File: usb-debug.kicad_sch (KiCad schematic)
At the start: 86 parts, among them IC1 AP22652W6-7, IC15 TPS7A0518PDBVT, IC16 AP22653W6-7, IC7 HD3SS3220, J11 632723300011, T10 BSS138APW, T6 BSS138APW, T7 BSS138APW, T9 BSS138APW

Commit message: Update local libraries
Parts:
- IC1: footprint antmicro-footprints:SOT-23-6 -> jetson-nano-baseboard-footprints:SOT-23-6; symbol antmicroPMICPowerDistributionSwitchesLoadDrivers:AP22652W6-7 -> jetson-nano-baseboard:AP22652W6-7

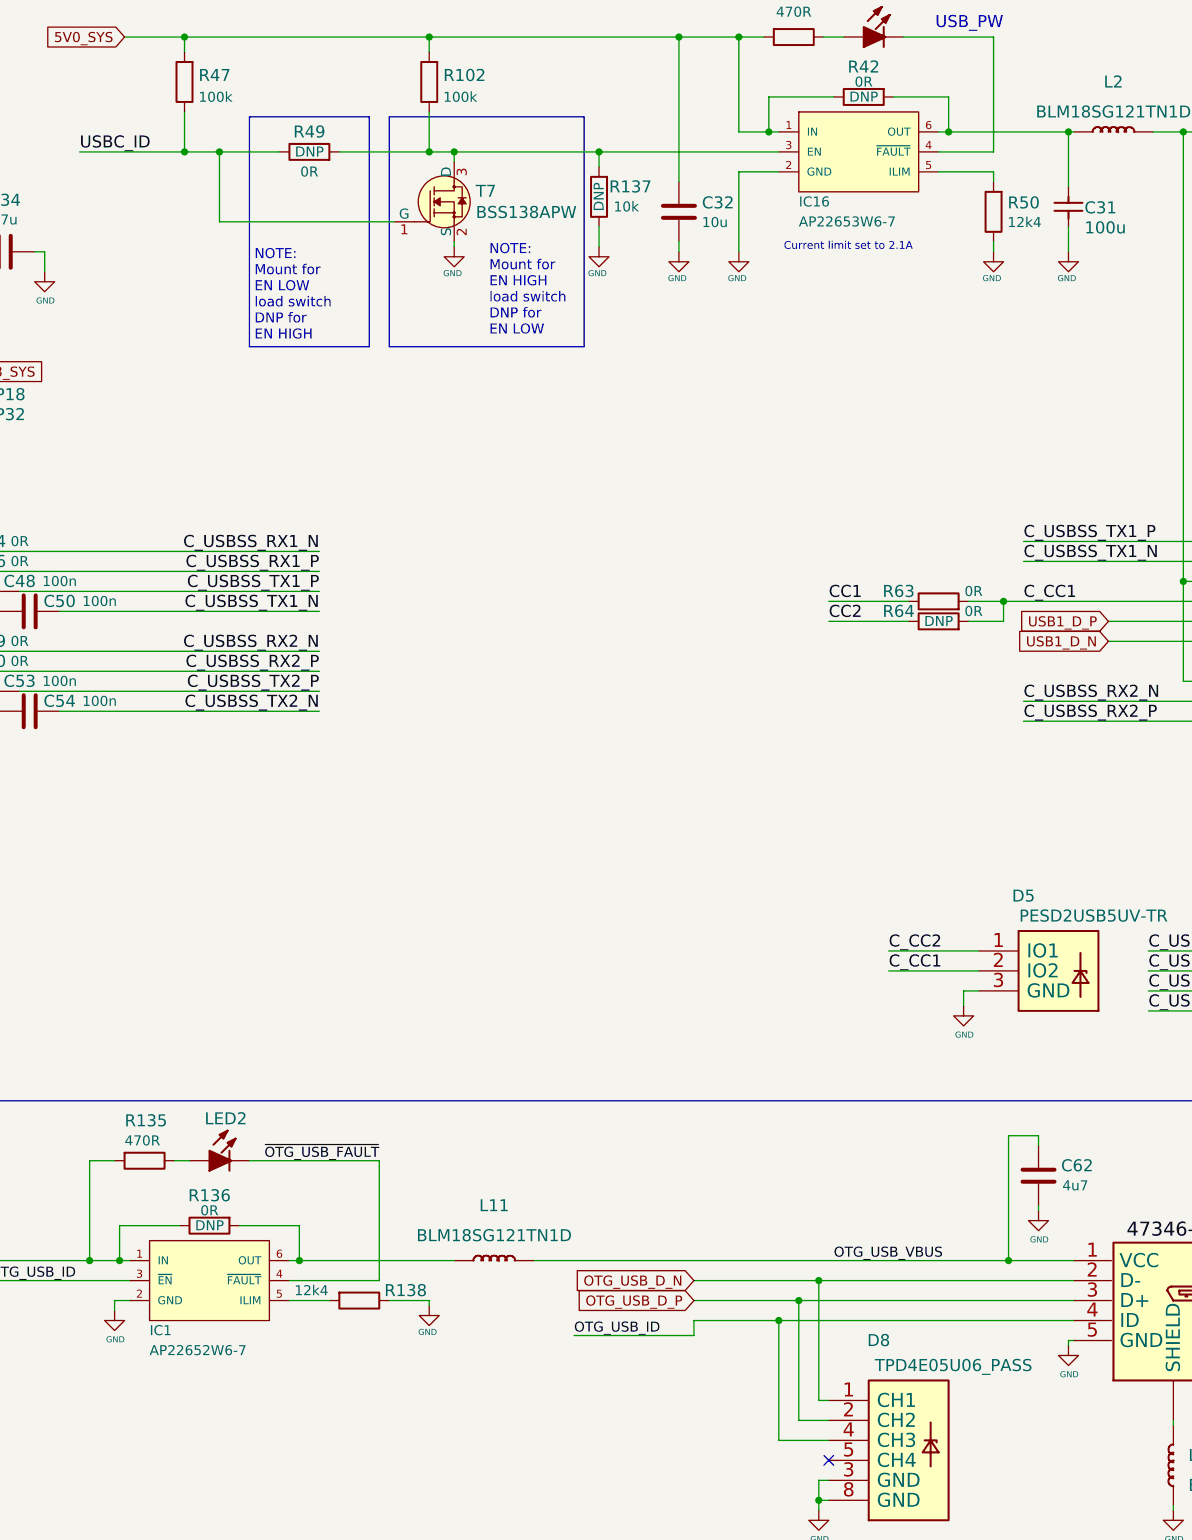
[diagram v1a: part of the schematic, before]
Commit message: Replace USB power switches with version without output discharge
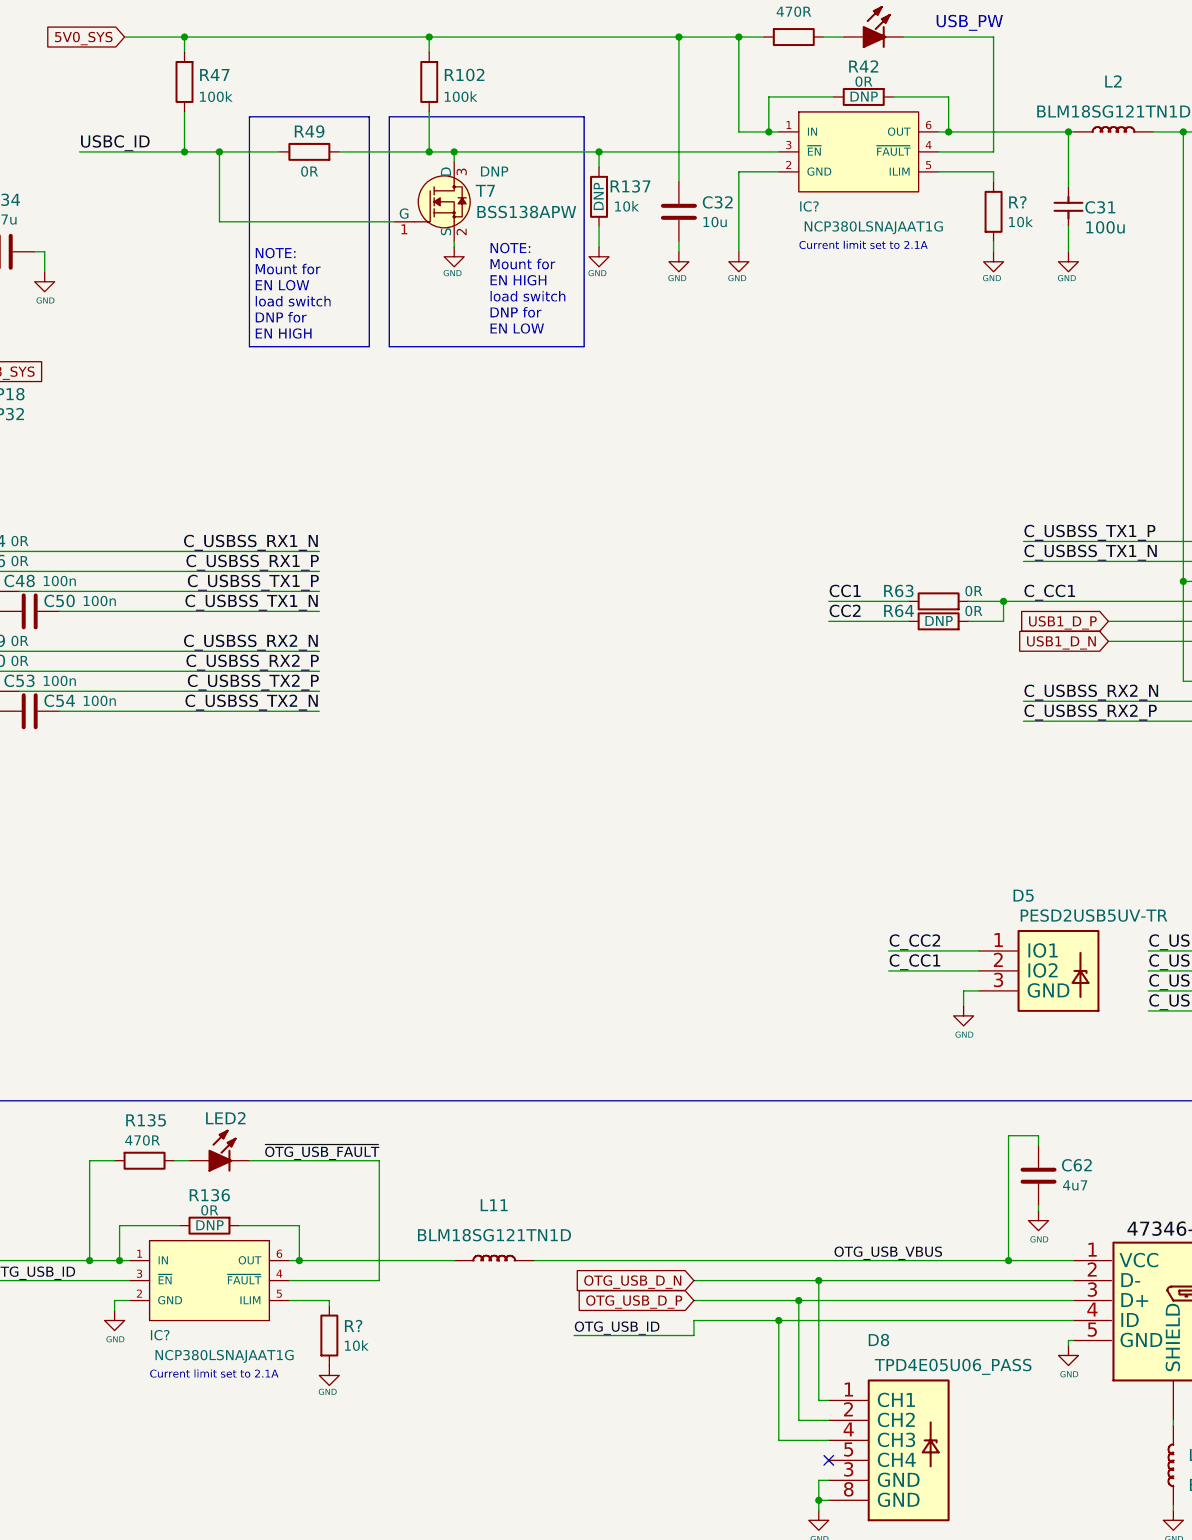
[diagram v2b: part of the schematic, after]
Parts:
- removed IC1: AP22652W6-7, jetson-nano-baseboard-footprints:SOT-23-6, symbol jetson-nano-baseboard:AP22652W6-7
- removed IC16: AP22653W6-7, jetson-nano-baseboard-footprints:SOT-23-6, symbol jetson-nano-baseboard:AP22653W6-7
- removed R138, R50: R_12k4_0402, jetson-nano-baseboard-footprints:0402-res, symbol jetson-nano-baseboard:R_12k4_0402
- added IC? (x2): NCP380LSNAJAAT1G, jetson-nano-baseboard-footprints:SOT-23-6, symbol jetson-nano-baseboard:NCP380LSNAJAAT1G
- added R? (x2): R_10k_0402, jetson-nano-baseboard-footprints:0402-res, symbol jetson-nano-baseboard:R_10k_0402
- R49: DNP DNP -> (none)
- T7: DNP (none) -> DNP
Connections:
- net 5V0_SYS: now also IC?.1 (IN), IC?.1 (IN)
- net GND: now also IC?.2 (GND), IC?.2 (GND), R?.2, R?.2
- net OTG_USB_ID: now also IC?.3 (~{EN})
- net ~{OTG_USB_FAULT}: now also IC?.4 (~{FAULT})
- net at C31.2, L2.1 (P), R42.2: now also IC?.6 (OUT)
- net at LED1.2 (K): now also IC?.4 (~{FAULT})
- net at R102.1, R137.2, R49.2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: now also IC?.3 (~{EN})
- net at L11.1 (P), R136.2: now also IC?.6 (OUT)
- new net: IC?.5 (ILIM), R?.1 (x2)

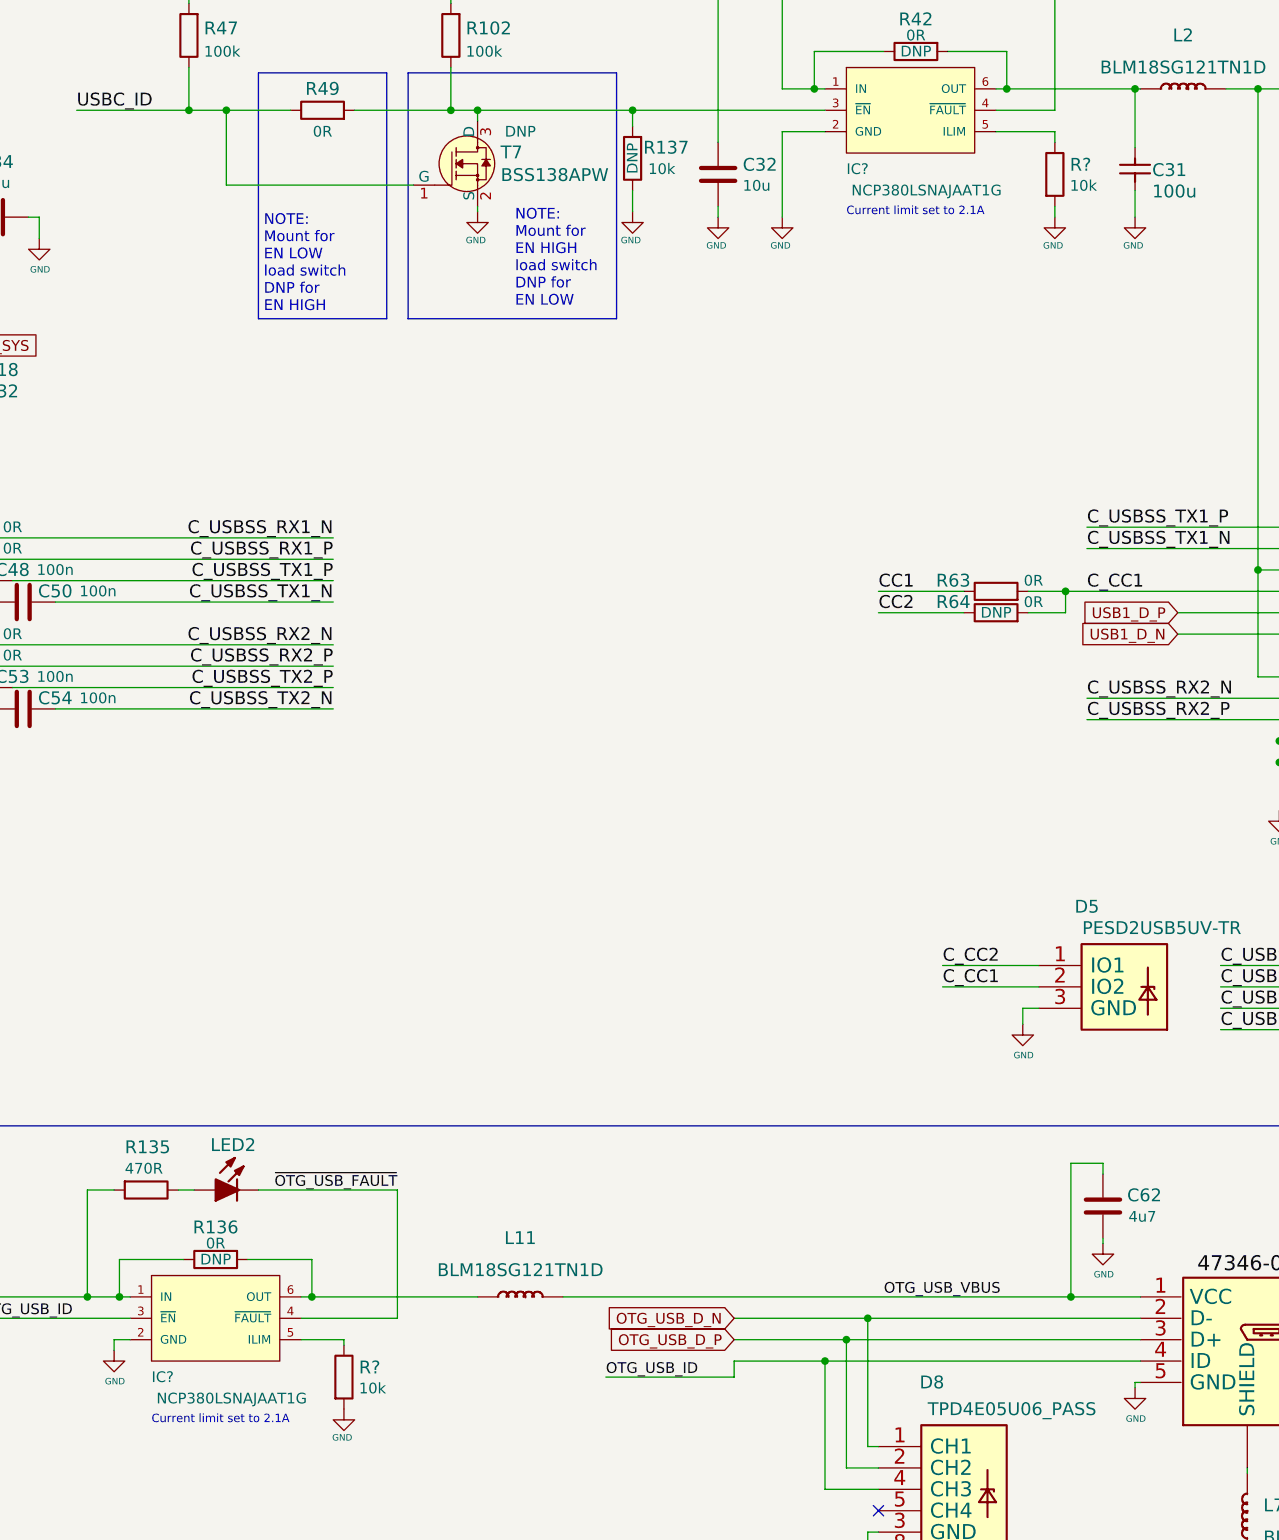
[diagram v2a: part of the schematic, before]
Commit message: Update parts enumeration
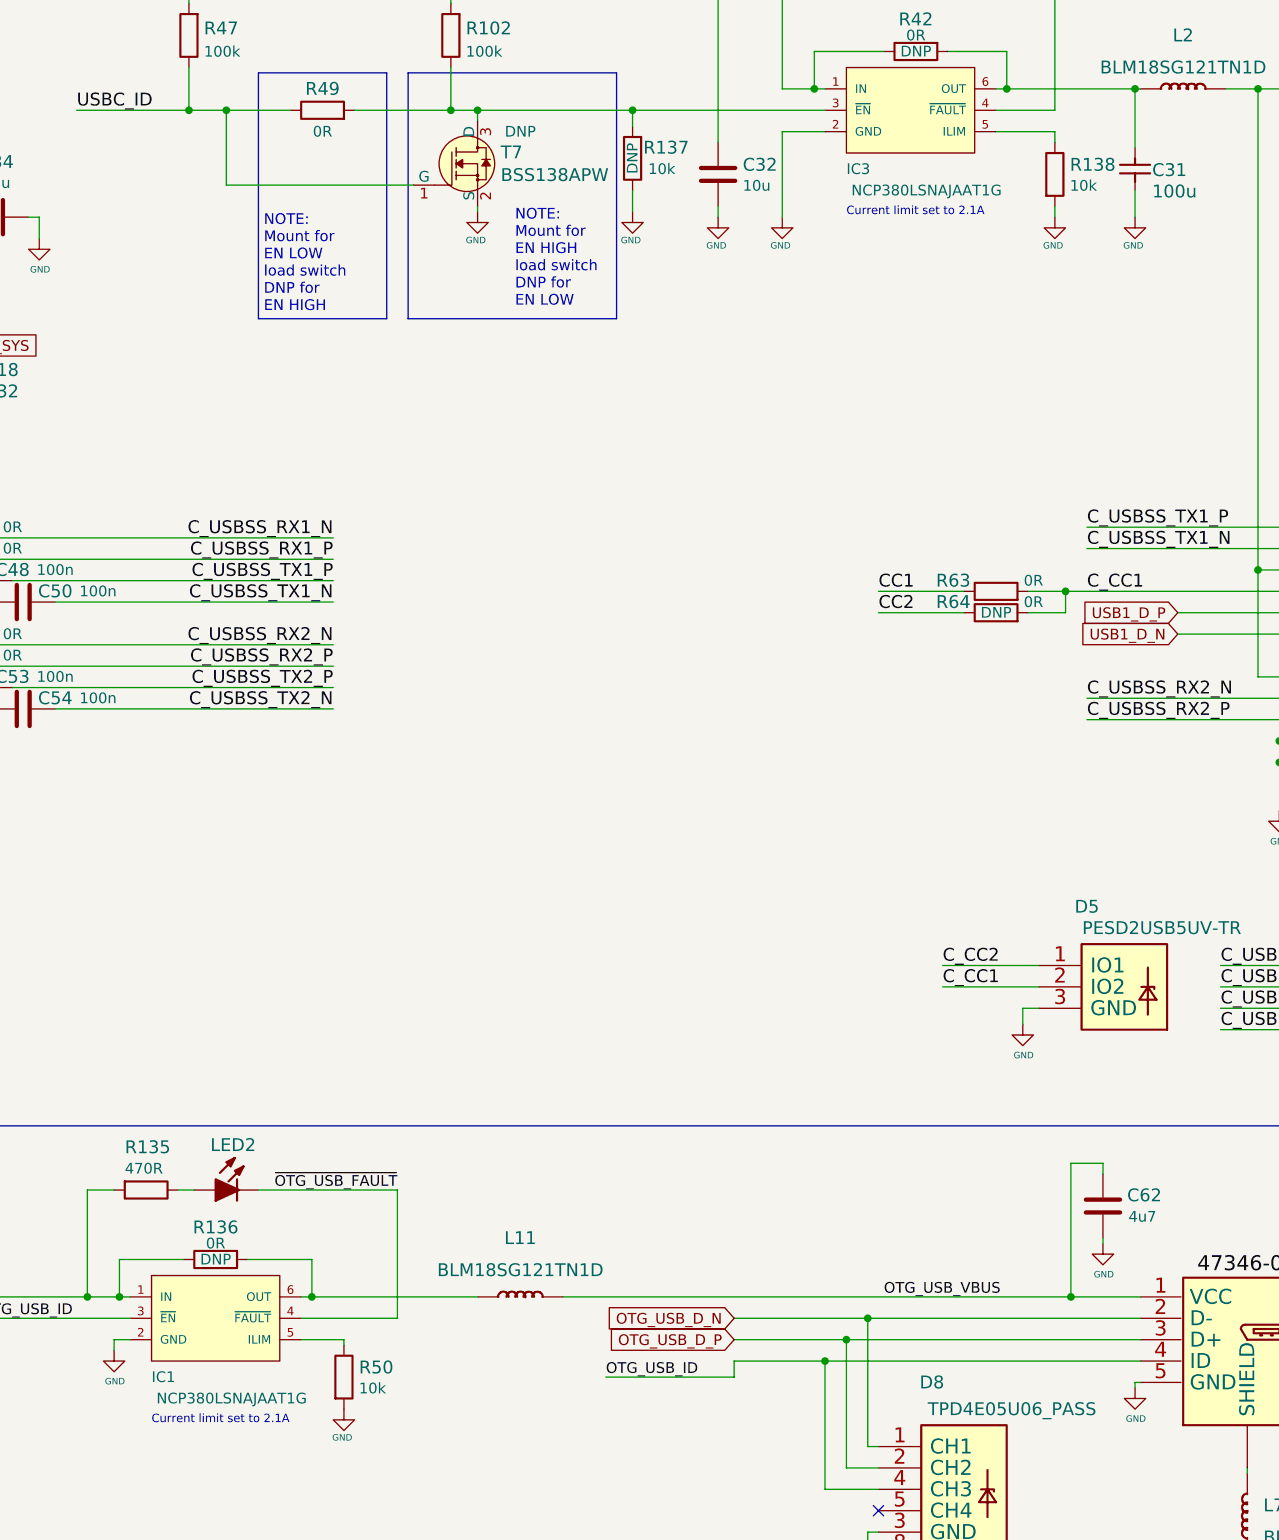
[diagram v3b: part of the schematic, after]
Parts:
- gave numbers to parts that had none: 4
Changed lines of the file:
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@@
   (symbol (lib_id "jetson-nano-baseboard:NCP380LSNAJAAT1G") (at 278.765 38.1 0) (unit 1)
     (in_bom yes) (on_board yes)
-    (property "Reference" "IC?" (id 0) (at 271.145 45.085 0)
+    (property "Reference" "IC3" (id 0) (at 271.145 45.085 0)
       (effects (font (size 1.27 1.27)) (justify left))
     )
@@
   (symbol (lib_id "jetson-nano-baseboard:R_10k_0402") (at 295.91 45.72 270) (unit 1)
     (in_bom yes) (on_board yes)
-    (property "Reference" "R?" (id 0) (at 297.688 44.577 90)
+    (property "Reference" "R138" (id 0) (at 297.688 44.577 90)
       (effects (font (size 1.524 1.524)) (justify left))
     )
@@
   (symbol (lib_id "jetson-nano-baseboard:NCP380LSNAJAAT1G") (at 196.215 181.61 0) (unit 1)
     (in_bom yes) (on_board yes)
-    (property "Reference" "IC?" (id 0) (at 188.595 188.595 0)
+    (property "Reference" "IC1" (id 0) (at 188.595 188.595 0)
       (effects (font (size 1.27 1.27)) (justify left))
     )
@@
   (symbol (lib_id "jetson-nano-baseboard:R_10k_0402") (at 211.455 188.595 270) (unit 1)
     (in_bom yes) (on_board yes)
-    (property "Reference" "R?" (id 0) (at 213.233 187.452 90)
-      (effects (font (size 1.524 1.524)) (justify left))
-    )
+    (property "Reference" "R50" (id 0) (at 213.233 187.452 90)
+      (effects (font (size 1.524 1.524)) (justify left))
+    )

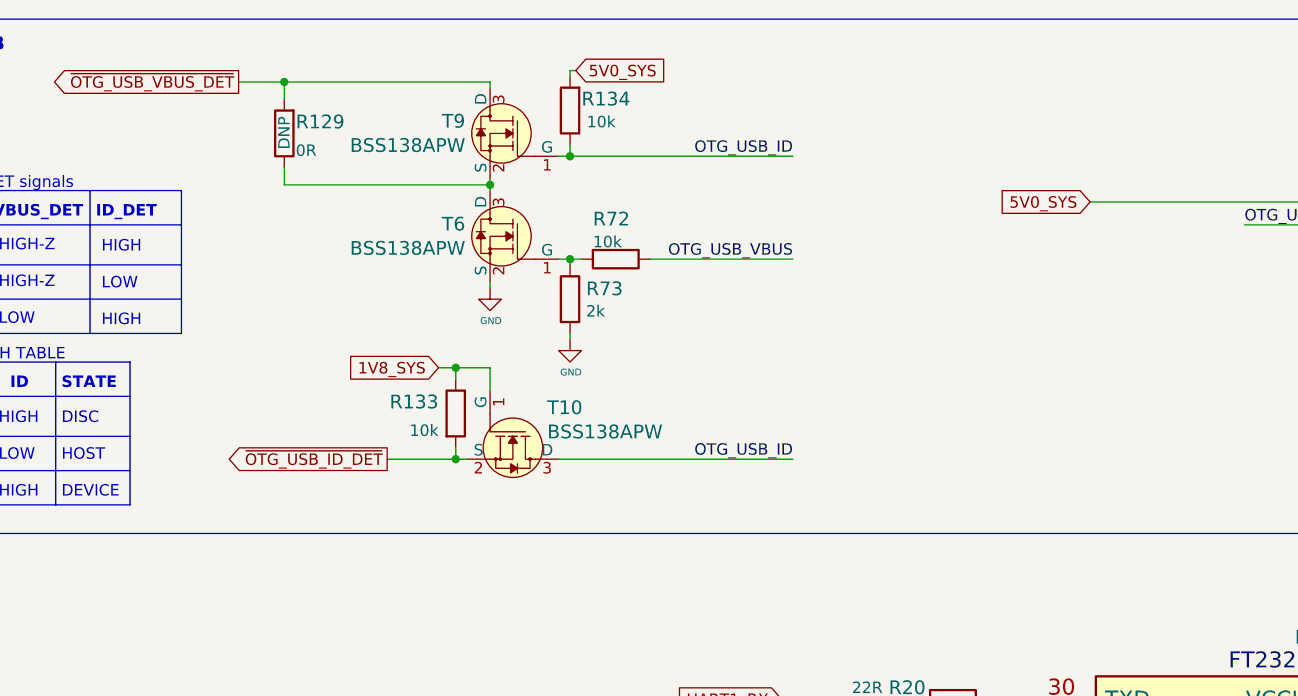
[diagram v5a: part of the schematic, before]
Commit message: Fix USB-OTG backfeed issue #44022
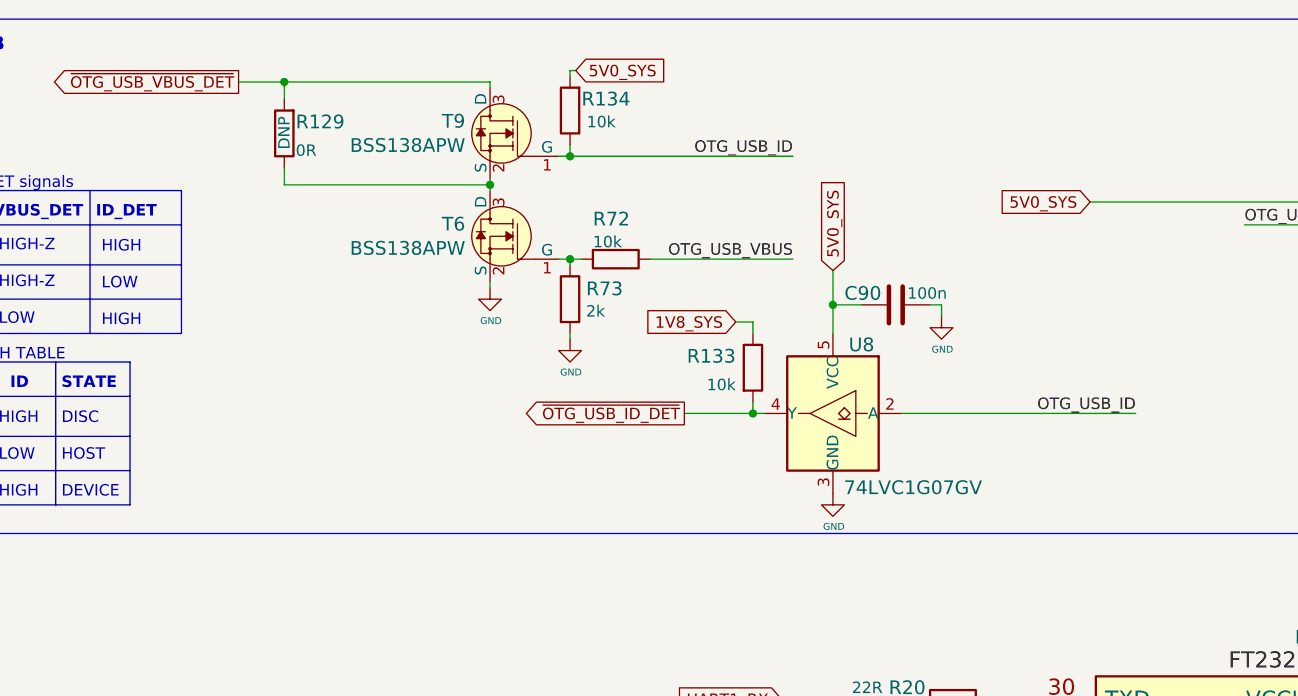
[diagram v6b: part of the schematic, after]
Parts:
- removed T10: BSS138APW, jetson-nano-baseboard-footprints:SC70-3, symbol jetson-nano-baseboard:BSS138APW
- added C90: C_100n_0402, jetson-nano-baseboard-footprints:0402-cap, symbol jetson-nano-baseboard:C_100n_0402
- added U8: 74LVC1G07GV, antmicro-footprints:SOT-753, symbol antmicroLogicBuffersDriversReceiversTransceivers:74LVC1G07GV
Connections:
- net 5V0_SYS: now also C90.2, U8.5 (VCC)
- net GND: now also C90.1, U8.3 (GND)
- net OTG_USB_ID: now also U8.2 (A)
- net ~{OTG_USB_ID_DET}: now also U8.4 (Y)
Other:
- moved on the sheet: R133
